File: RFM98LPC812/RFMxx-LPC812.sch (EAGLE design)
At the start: 24 parts, among them X1 BU-SMA-V, X2 BU-SMA-V

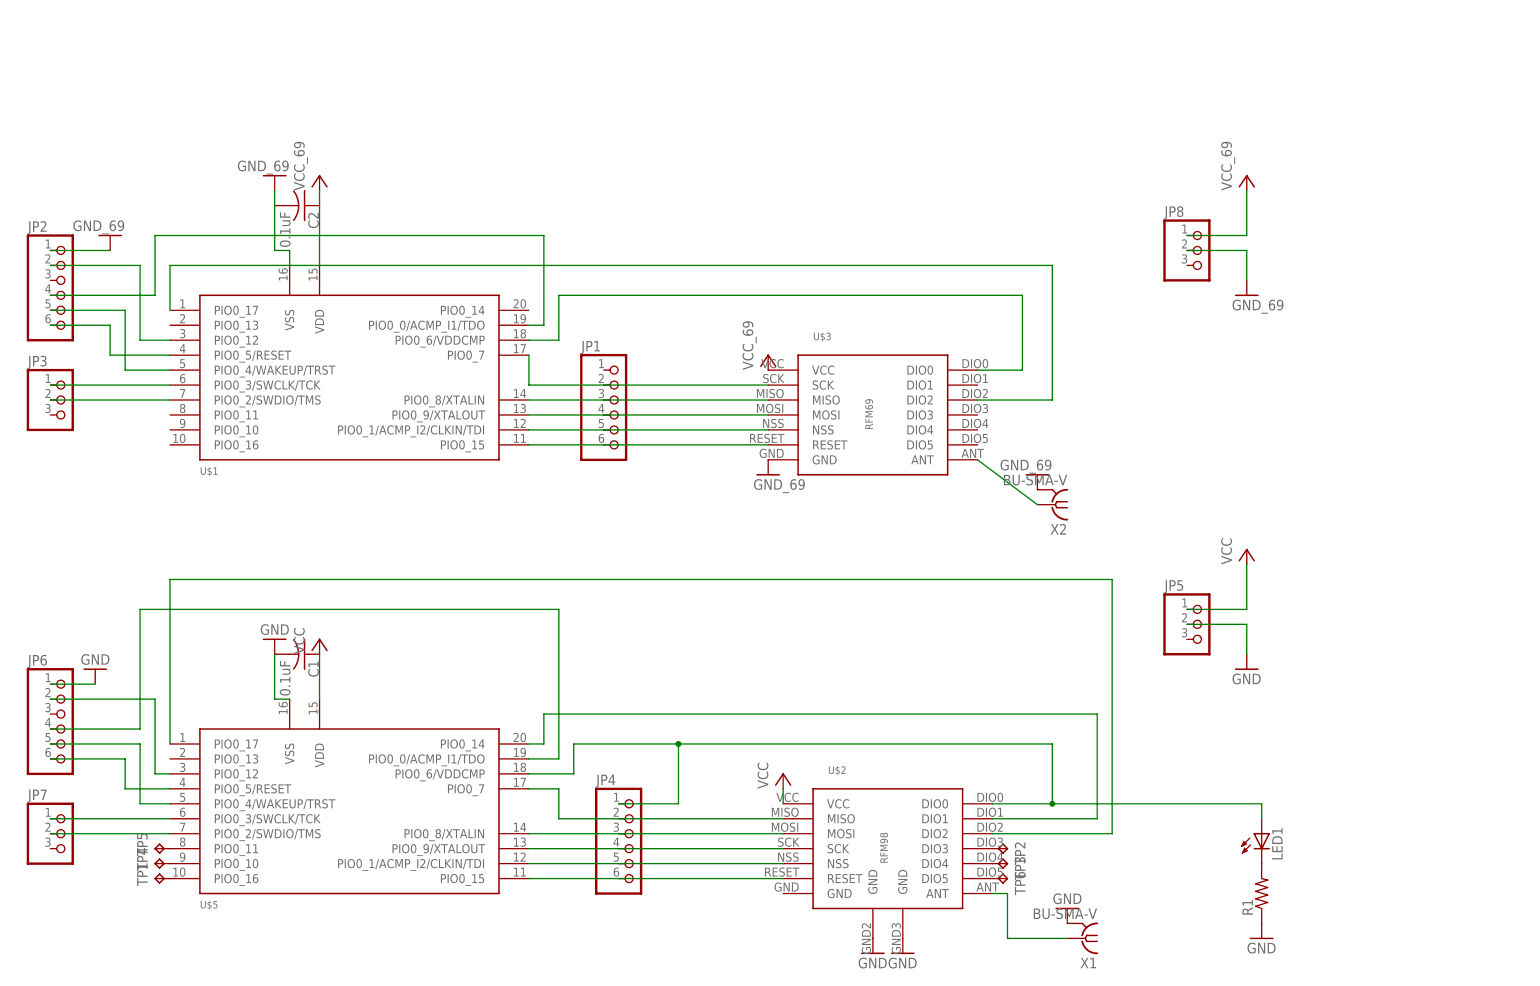
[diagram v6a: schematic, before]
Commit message: trace bug fixes
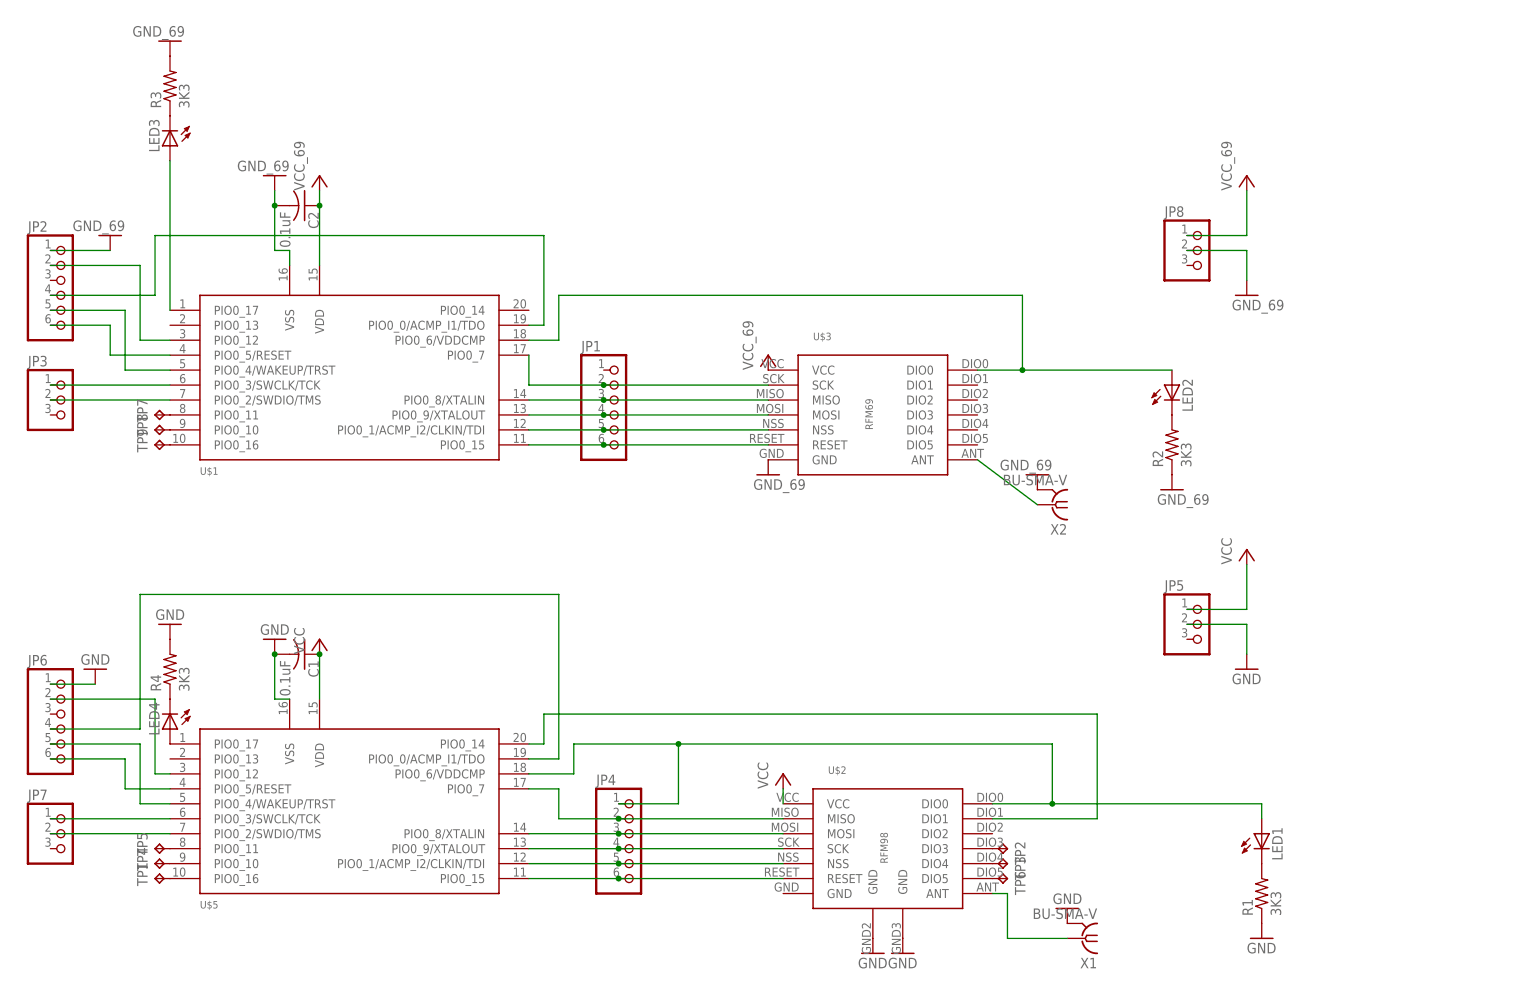
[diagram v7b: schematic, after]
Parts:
- added LED2, LED3, LED4: (no value), adafruit:LEDCHIP-LED0805
- added R2, R3, R4: 3K3, resistor:R-US_R0805
- added TP7, TP8, TP9: TPB1,27, testpad:TPB1,27
- R1: value (none) -> 3K3
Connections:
- new net N$38: LED2.C, R2.2
- new net N$39: LED3.C, R3.1
- new net N$41: TP7.TP, U$1.PIO0_11
- new net N$42: LED4.C, R4.1
- new net N$43: TP8.TP, U$1.PIO0_10
- new net N$44: TP9.TP, U$1.PIO0_16
- net GND: now also R2.1, R3.2, R4.2
- net N$24: now also LED2.A
- net N$26: now also LED4.A; no longer U$2.DIO2
- net N$36: now also LED3.A; no longer U$3.DIO2
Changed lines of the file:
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@@
 <part name="LED1" library="adafruit" deviceset="LED" device="CHIP-LED0805"/>
 <part name="GND_RFM4" library="supply1" deviceset="GND" device=""/>
-<part name="R1" library="resistor" deviceset="R-US_" device="R0805"/>
+<part name="R1" library="resistor" deviceset="R-US_" device="R0805" value="3K3"/>
+<part name="LED2" library="adafruit" deviceset="LED" device="CHIP-LED0805"/>
+<part name="R2" library="resistor" deviceset="R-US_" device="R0805" value="3K3"/>
+<part name="GND6" library="supply1" deviceset="GND" device="" value="GND_69"/>
+<part name="LED3" library="adafruit" deviceset="LED" device="CHIP-LED0805"/>
+<part name="R3" library="resistor" deviceset="R-US_" device="R0805" value="3K3"/>
+<part name="GND7" library="supply1" deviceset="GND" device="" value="GND_69"/>
+<part name="LED4" library="adafruit" deviceset="LED" device="CHIP-LED0805"/>
+<part name="R4" library="resistor" deviceset="R-US_" device="R0805" value="3K3"/>
+<part name="GND_RFM6" library="supply1" deviceset="GND" device=""/>
+<part name="TP7" library="testpad" deviceset="TP" device="B1,27"/>
+<part name="TP8" library="testpad" deviceset="TP" device="B1,27"/>
+<part name="TP9" library="testpad" deviceset="TP" device="B1,27"/>
 </parts>
 <sheets>
@@
 <instance part="GND_RFM4" gate="1" x="66.04" y="-48.26"/>
 <instance part="R1" gate="G$1" x="66.04" y="-40.64" rot="R90"/>
+<instance part="LED2" gate="G$1" x="50.8" y="45.72"/>
+<instance part="R2" gate="G$1" x="50.8" y="35.56" rot="R90"/>
+<instance part="GND6" gate="1" x="50.8" y="27.94"/>
+<instance part="LED3" gate="G$1" x="-119.38" y="86.36" rot="R180"/>
+<instance part="R3" gate="G$1" x="-119.38" y="96.52" rot="R90"/>
+<instance part="GND7" gate="1" x="-119.38" y="104.14" rot="R180"/>
+<instance part="LED4" gate="G$1" x="-119.38" y="-12.7" rot="R180"/>
+<instance part="R4" gate="G$1" x="-119.38" y="-2.54" rot="R90"/>
+<instance part="GND_RFM6" gate="1" x="-119.38" y="5.08" rot="R180"/>
+<instance part="TP7" gate="G$1" x="-121.92" y="40.64" rot="R90"/>
+<instance part="TP8" gate="G$1" x="-121.92" y="38.1" rot="R90"/>
+<instance part="TP9" gate="G$1" x="-121.92" y="35.56" rot="R90"/>
 </instances>
 <busses>
@@
 <pinref part="U$5" gate="G$1" pin="VDD"/>
 <wire x1="-93.98" y1="-7.62" x2="-93.98" y2="0" width="0.1524" layer="91"/>
+<junction x="-93.98" y="0"/>
 </segment>
 <segment>
@@
 <wire x1="-93.98" y1="78.74" x2="-93.98" y2="76.2" width="0.1524" layer="91"/>
 <pinref part="P+2" gate="VCC" pin="VCC"/>
+<junction x="-93.98" y="76.2"/>
 </segment>
 <segment>
@@
 <pinref part="U$2" gate="G$1" pin="MOSI"/>
 <wire x1="-43.18" y1="-30.48" x2="-15.24" y2="-30.48" width="0.1524" layer="91"/>
+<junction x="-43.18" y="-30.48"/>
 </segment>
 </net>
@@
 <pinref part="U$2" gate="G$1" pin="SCK"/>
 <wire x1="-43.18" y1="-33.02" x2="-15.24" y2="-33.02" width="0.1524" layer="91"/>
+<junction x="-43.18" y="-33.02"/>
 </segment>
 </net>
@@
 <pinref part="U$2" gate="G$1" pin="RESET"/>
 <wire x1="-43.18" y1="-38.1" x2="-15.24" y2="-38.1" width="0.1524" layer="91"/>
+<junction x="-43.18" y="-38.1"/>
 </segment>
 </net>
@@
 <pinref part="U$3" gate="G$1" pin="RESET"/>
 <wire x1="-45.72" y1="35.56" x2="-17.78" y2="35.56" width="0.1524" layer="91"/>
+<junction x="-45.72" y="35.56"/>
 </segment>
 </net>
@@
 <pinref part="U$3" gate="G$1" pin="NSS"/>
 <wire x1="-45.72" y1="38.1" x2="-17.78" y2="38.1" width="0.1524" layer="91"/>
+<junction x="-45.72" y="38.1"/>
 </segment>
 </net>
@@
 <pinref part="U$3" gate="G$1" pin="MOSI"/>
 <wire x1="-45.72" y1="40.64" x2="-17.78" y2="40.64" width="0.1524" layer="91"/>
+<junction x="-45.72" y="40.64"/>
 </segment>
 </net>
@@
 <pinref part="U$3" gate="G$1" pin="MISO"/>
 <wire x1="-45.72" y1="43.18" x2="-17.78" y2="43.18" width="0.1524" layer="91"/>
+<junction x="-45.72" y="43.18"/>
 </segment>
 </net>
@@
 <pinref part="U$3" gate="G$1" pin="SCK"/>
 <wire x1="-45.72" y1="45.72" x2="-17.78" y2="45.72" width="0.1524" layer="91"/>
+<junction x="-45.72" y="45.72"/>
 </segment>
 </net>
@@
 <pinref part="U$2" gate="G$1" pin="NSS"/>
 <wire x1="-43.18" y1="-35.56" x2="-15.24" y2="-35.56" width="0.1524" layer="91"/>
+<junction x="-43.18" y="-35.56"/>
 </segment>
 </net>
@@
 <wire x1="-99.06" y1="-7.62" x2="-101.6" y2="-7.62" width="0.1524" layer="91"/>
 <wire x1="-101.6" y1="-7.62" x2="-101.6" y2="0" width="0.1524" layer="91"/>
+<junction x="-101.6" y="0"/>
 </segment>
 <segment>
@@
 <wire x1="-101.6" y1="78.74" x2="-101.6" y2="76.2" width="0.1524" layer="91"/>
 <pinref part="GND2" gate="1" pin="GND"/>
+<junction x="-101.6" y="76.2"/>
 </segment>
 <segment>
 <pinref part="GND_RFM4" gate="1" pin="GND"/>
 <pinref part="R1" gate="G$1" pin="1"/>
+</segment>
+<segment>
+<pinref part="R2" gate="G$1" pin="1"/>
+<pinref part="GND6" gate="1" pin="GND"/>
+</segment>
+<segment>
+<pinref part="R3" gate="G$1" pin="2"/>
+<pinref part="GND7" gate="1" pin="GND"/>
+</segment>
+<segment>
+<pinref part="R4" gate="G$1" pin="2"/>
+<pinref part="GND_RFM6" gate="1" pin="GND"/>
 </segment>
 </net>
@@
 <pinref part="U$2" gate="G$1" pin="MISO"/>
 <wire x1="-43.18" y1="-27.94" x2="-15.24" y2="-27.94" width="0.1524" layer="91"/>
+<junction x="-43.18" y="-27.94"/>
 </segment>
 </net>
@@
 <net name="N$20" class="0">
 <segment>
-<wire x1="-124.46" y1="-12.7" x2="-124.46" y2="7.62" width="0.1524" layer="91"/>
-<wire x1="-124.46" y1="7.62" x2="-53.34" y2="7.62" width="0.1524" layer="91"/>
-<wire x1="-53.34" y1="7.62" x2="-53.34" y2="-17.78" width="0.1524" layer="91"/>
+<wire x1="-124.46" y1="-12.7" x2="-124.46" y2="10.16" width="0.1524" layer="91"/>
+<wire x1="-124.46" y1="10.16" x2="-53.34" y2="10.16" width="0.1524" layer="91"/>
+<wire x1="-53.34" y1="10.16" x2="-53.34" y2="-17.78" width="0.1524" layer="91"/>
 <pinref part="U$5" gate="G$1" pin="PIO0_0/ACMP_I1/TDO"/>
 <wire x1="-53.34" y1="-17.78" x2="-58.42" y2="-17.78" width="0.1524" layer="91"/>
@@
 </segment>
 </net>
-<net name="N$26" class="0">
-<segment>
-<pinref part="U$5" gate="G$1" pin="PIO0_17"/>
-<wire x1="-119.38" y1="-15.24" x2="-119.38" y2="12.7" width="0.1524" layer="91"/>
-<wire x1="-119.38" y1="12.7" x2="40.64" y2="12.7" width="0.1524" layer="91"/>
-<wire x1="40.64" y1="12.7" x2="40.64" y2="-30.48" width="0.1524" layer="91"/>
-<pinref part="U$2" gate="G$1" pin="DIO2"/>
-<wire x1="40.64" y1="-30.48" x2="20.32" y2="-30.48" width="0.1524" layer="91"/>
-</segment>
-</net>
 <net name="N$27" class="0">
 <segment>
@@
 <pinref part="U$1" gate="G$1" pin="PIO0_6/VDDCMP"/>
 <wire x1="-53.34" y1="53.34" x2="-58.42" y2="53.34" width="0.1524" layer="91"/>
-</segment>
-</net>
-<net name="N$36" class="0">
-<segment>
-<pinref part="U$3" gate="G$1" pin="DIO2"/>
-<wire x1="17.78" y1="43.18" x2="30.48" y2="43.18" width="0.1524" layer="91"/>
-<wire x1="30.48" y1="43.18" x2="30.48" y2="66.04" width="0.1524" layer="91"/>
-<wire x1="30.48" y1="66.04" x2="-119.38" y2="66.04" width="0.1524" layer="91"/>
-<pinref part="U$1" gate="G$1" pin="PIO0_17"/>
-<wire x1="-119.38" y1="66.04" x2="-119.38" y2="58.42" width="0.1524" layer="91"/>
+<pinref part="LED2" gate="G$1" pin="A"/>
+<wire x1="25.4" y1="48.26" x2="50.8" y2="48.26" width="0.1524" layer="91"/>
+<junction x="25.4" y="48.26"/>
 </segment>
 </net>
@@
 </segment>
 </net>
+<net name="N$38" class="0">
+<segment>
+<pinref part="LED2" gate="G$1" pin="C"/>
+<pinref part="R2" gate="G$1" pin="2"/>
+</segment>
+</net>
+<net name="N$36" class="0">
+<segment>
+<pinref part="LED3" gate="G$1" pin="A"/>
+<pinref part="U$1" gate="G$1" pin="PIO0_17"/>
+<wire x1="-119.38" y1="83.82" x2="-119.38" y2="58.42" width="0.1524" layer="91"/>
+</segment>
+</net>
+<net name="N$39" class="0">
+<segment>
+<pinref part="LED3" gate="G$1" pin="C"/>
+<pinref part="R3" gate="G$1" pin="1"/>
+</segment>
+</net>
+<net name="N$42" class="0">
+<segment>
+<pinref part="LED4" gate="G$1" pin="C"/>
+<pinref part="R4" gate="G$1" pin="1"/>
+</segment>
+</net>
+<net name="N$26" class="0">
+<segment>
+<pinref part="U$5" gate="G$1" pin="PIO0_17"/>
+<pinref part="LED4" gate="G$1" pin="A"/>
+</segment>
+</net>
+<net name="N$41" class="0">
+<segment>
+<pinref part="U$1" gate="G$1" pin="PIO0_11"/>
+<pinref part="TP7" gate="G$1" pin="TP"/>
+</segment>
+</net>
+<net name="N$43" class="0">
+<segment>
+<pinref part="U$1" gate="G$1" pin="PIO0_10"/>
+<pinref part="TP8" gate="G$1" pin="TP"/>
+</segment>
+</net>
+<net name="N$44" class="0">
+<segment>
+<pinref part="U$1" gate="G$1" pin="PIO0_16"/>
+<pinref part="TP9" gate="G$1" pin="TP"/>
+</segment>
+</net>
